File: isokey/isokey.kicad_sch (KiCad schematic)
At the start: 3 parts, among them J1 PadExp Left, J2 PadExp Right, U1 BlackPill_STLINK

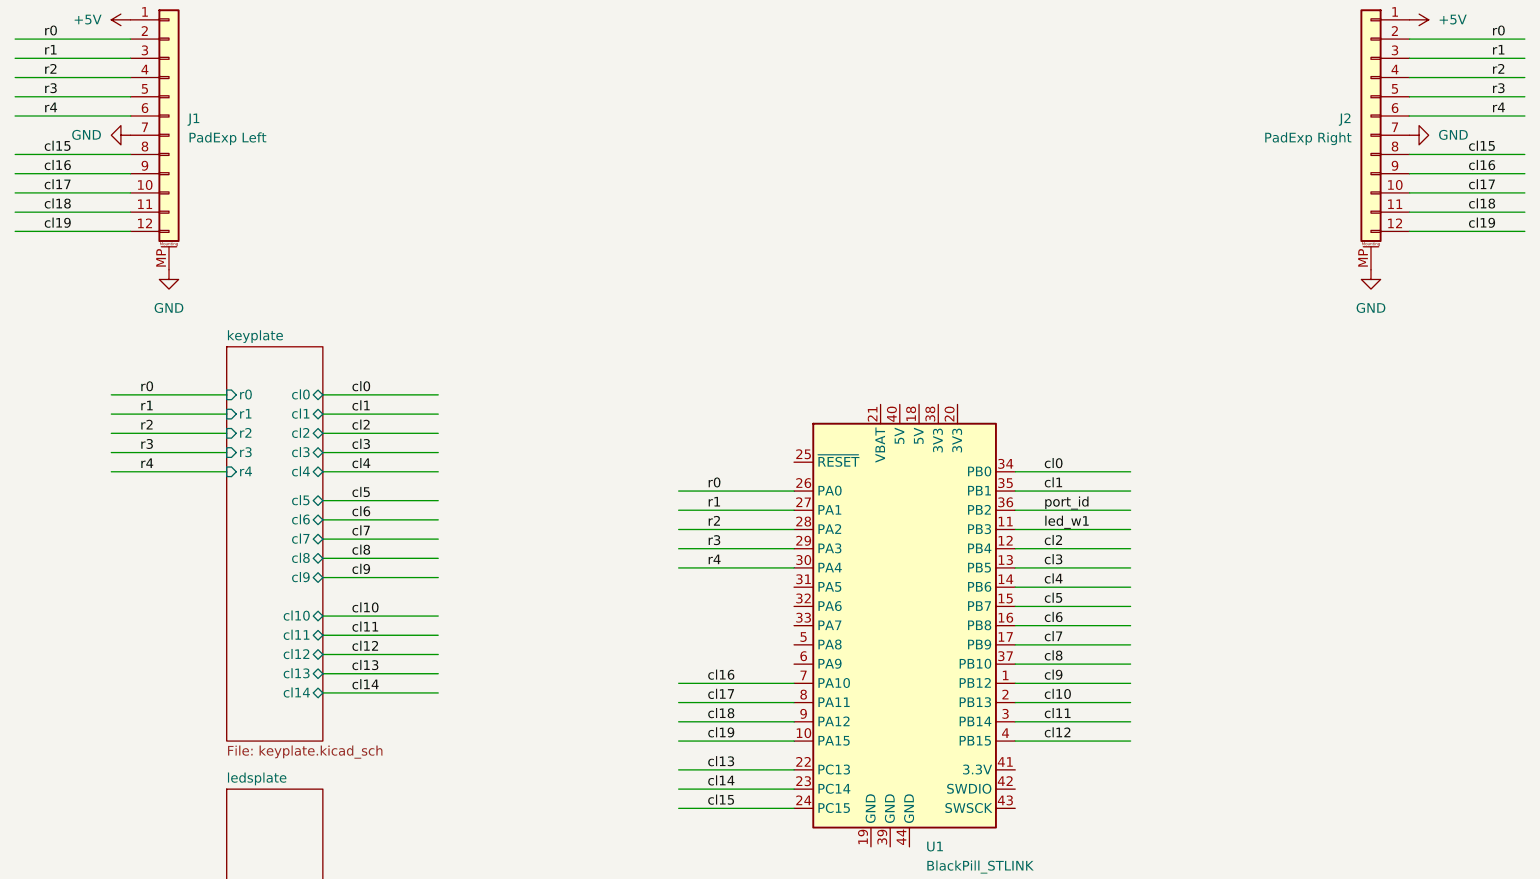
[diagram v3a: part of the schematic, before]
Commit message: Complete led wire
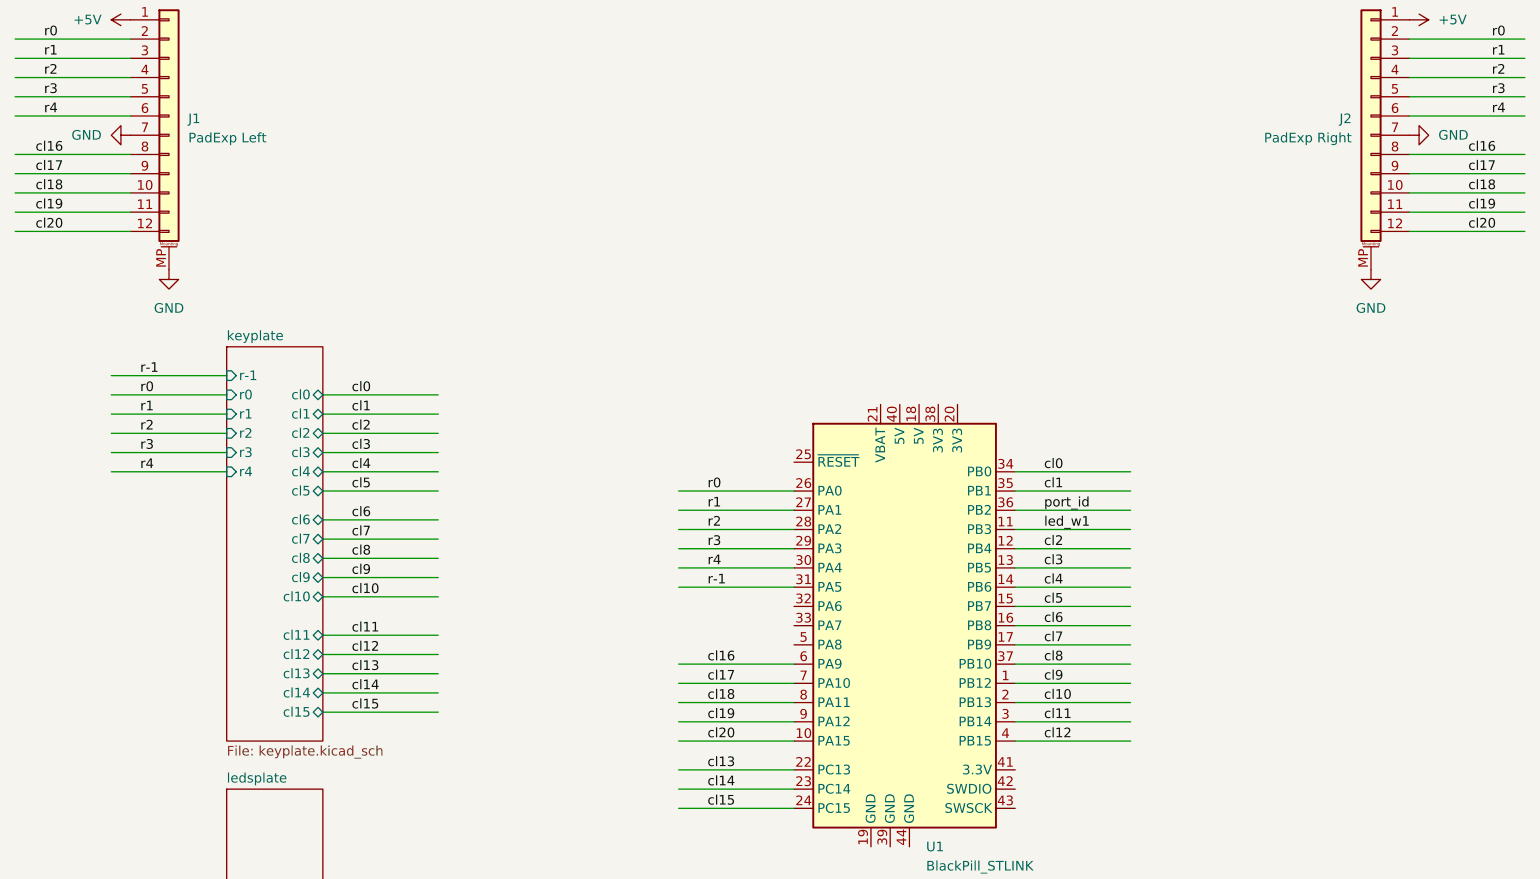
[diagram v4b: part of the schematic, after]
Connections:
- net cl15: no longer J1.8 (Pin_8), J2.8 (Pin_8)
- net cl16: now also J1.8 (Pin_8), J2.8 (Pin_8), U1.6 (PA9); no longer J1.9 (Pin_9), J2.9 (Pin_9), U1.7 (PA10)
- net cl17: now also J1.9 (Pin_9), J2.9 (Pin_9), U1.7 (PA10); no longer J1.10 (Pin_10), J2.10 (Pin_10), U1.8 (PA11)
- net cl18: now also J1.10 (Pin_10), J2.10 (Pin_10), U1.8 (PA11); no longer J1.11 (Pin_11), J2.11 (Pin_11), U1.9 (PA12)
- net cl19: now also J1.11 (Pin_11), J2.11 (Pin_11), U1.9 (PA12); no longer J1.12 (Pin_12), J2.12 (Pin_12), U1.10 (PA15)
- net r-1: now reaches U1.31 (PA5)
- new net cl20: J1.12 (Pin_12), J2.12 (Pin_12), U1.10 (PA15)
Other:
- sheet keyplate ports: added cl15, r-1; removed none

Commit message: Continue routing
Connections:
- net GND: now also U1.19 (GND), U1.39 (GND), U1.44 (GND)
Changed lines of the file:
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@@
     (company "IsoKey - asterix24@gmail.com")
   )
+  (junction (at 168.91 133.35) (diameter 0) (color 0 0 0 0)
+  )
+  (junction (at 171.45 133.35) (diameter 0) (color 0 0 0 0)
+  )
   (wire (pts (xy 187.96 93.98) (xy 203.2 93.98))
     (stroke (width 0) (type default))
@@
     (stroke (width 0) (type default))
   )
+  (wire (pts (xy 168.91 133.35) (xy 171.45 133.35))
+    (stroke (width 0) (type default))
+  )
   (wire (pts (xy 255.27 44.45) (xy 240.03 44.45))
     (stroke (width 0) (type default))
@@
   )
   (wire (pts (xy 96.52 105.41) (xy 111.76 105.41))
+    (stroke (width 0) (type default))
+  )
+  (wire (pts (xy 171.45 133.35) (xy 173.99 133.35))
     (stroke (width 0) (type default))
   )
@@
         )
       )
+    )
+  )
+  (symbol (lib_id "power:GND") (at 168.91 133.35 0) (unit 1)
+    (in_bom yes) (on_board yes) (dnp no) (fields_autoplaced)
+    (property "Reference" "#PWR0239" (at 168.91 139.7 0)
+      (effects (font (size 1.27 1.27)) hide)
+    )
+    (property "Value" "GND" (at 168.91 138.43 0)
+      (effects (font (size 1.27 1.27)))
+    )
+    (property "Footprint" "" (at 168.91 133.35 0)
+      (effects (font (size 1.27 1.27)) hide)
+    )
+    (property "Datasheet" "" (at 168.91 133.35 0)
+      (effects (font (size 1.27 1.27)) hide)
+    )
+    (pin "1")
+    (instances
+      (project "isokey"
+        (path "/b0c352a4-2db1-45ff-8668-f2efdeb7d408"
+          (reference "#PWR0239") (unit 1)
+        )
+      )

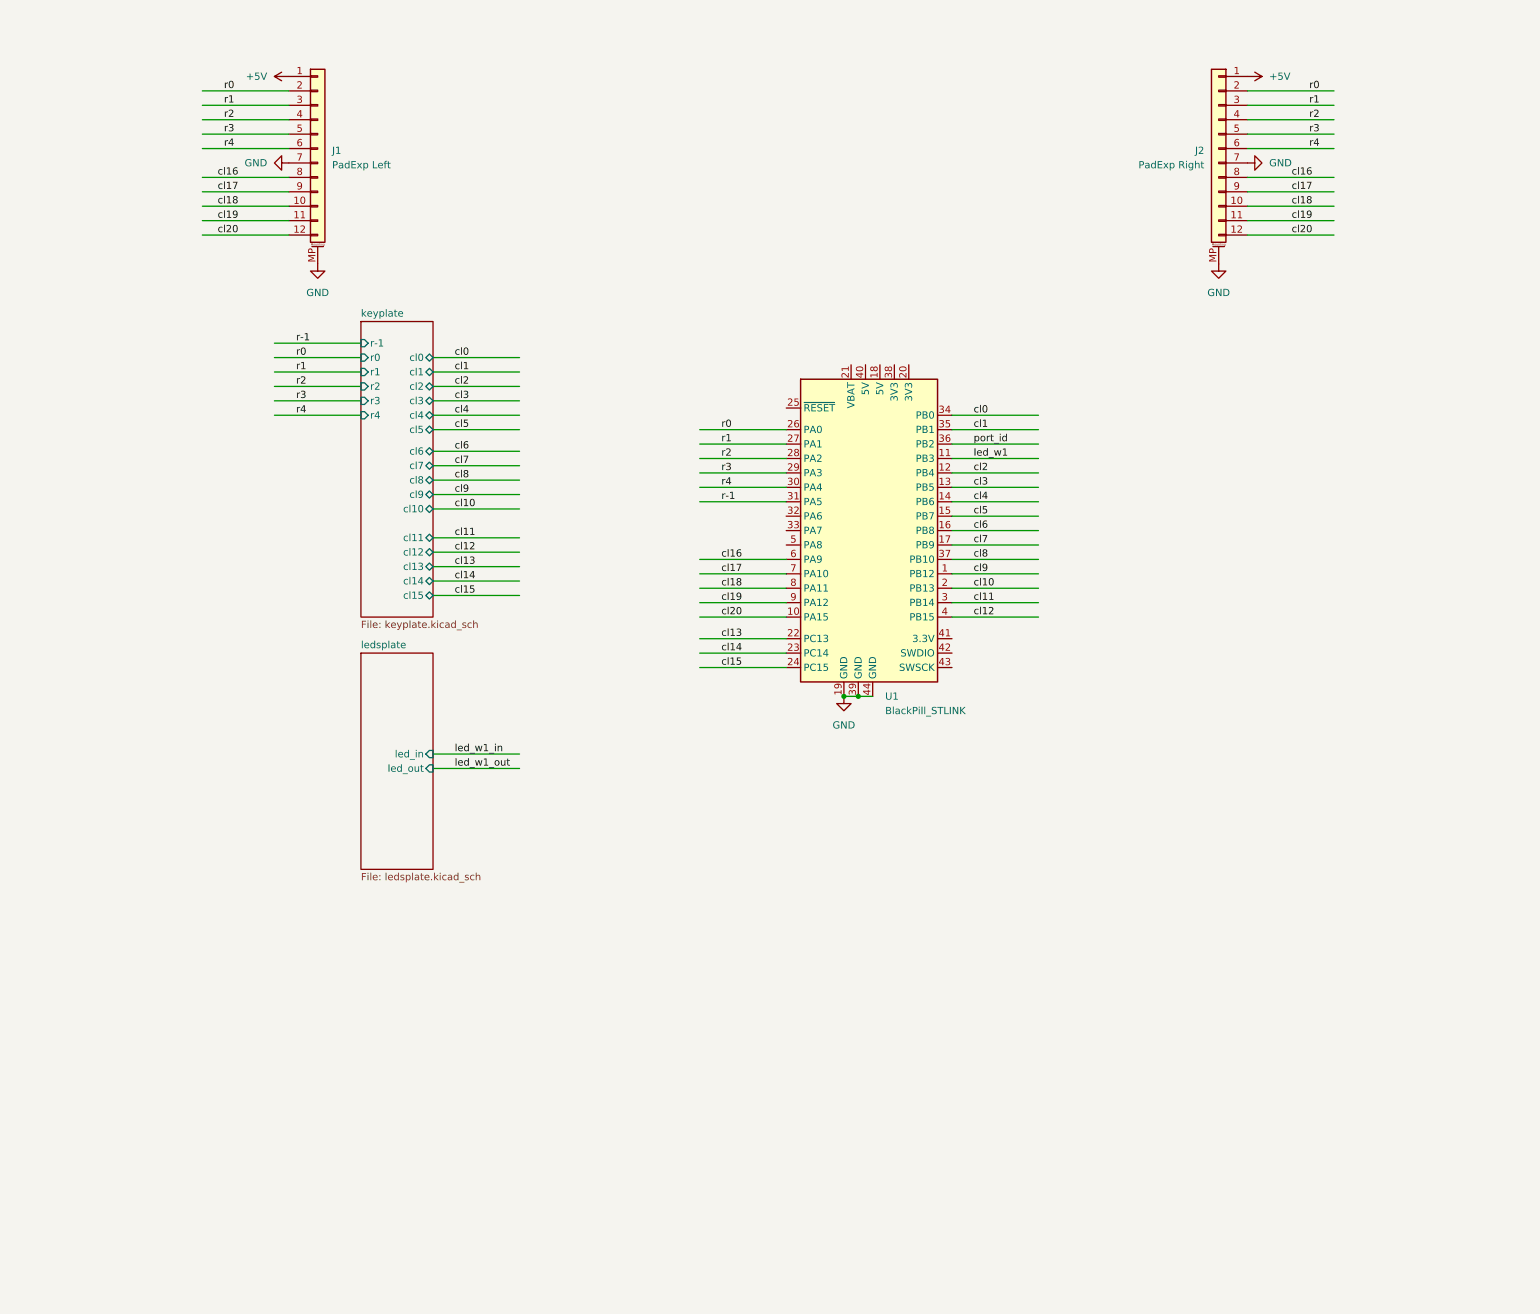
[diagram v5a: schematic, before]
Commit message: Add lp5569 chip and encoder.
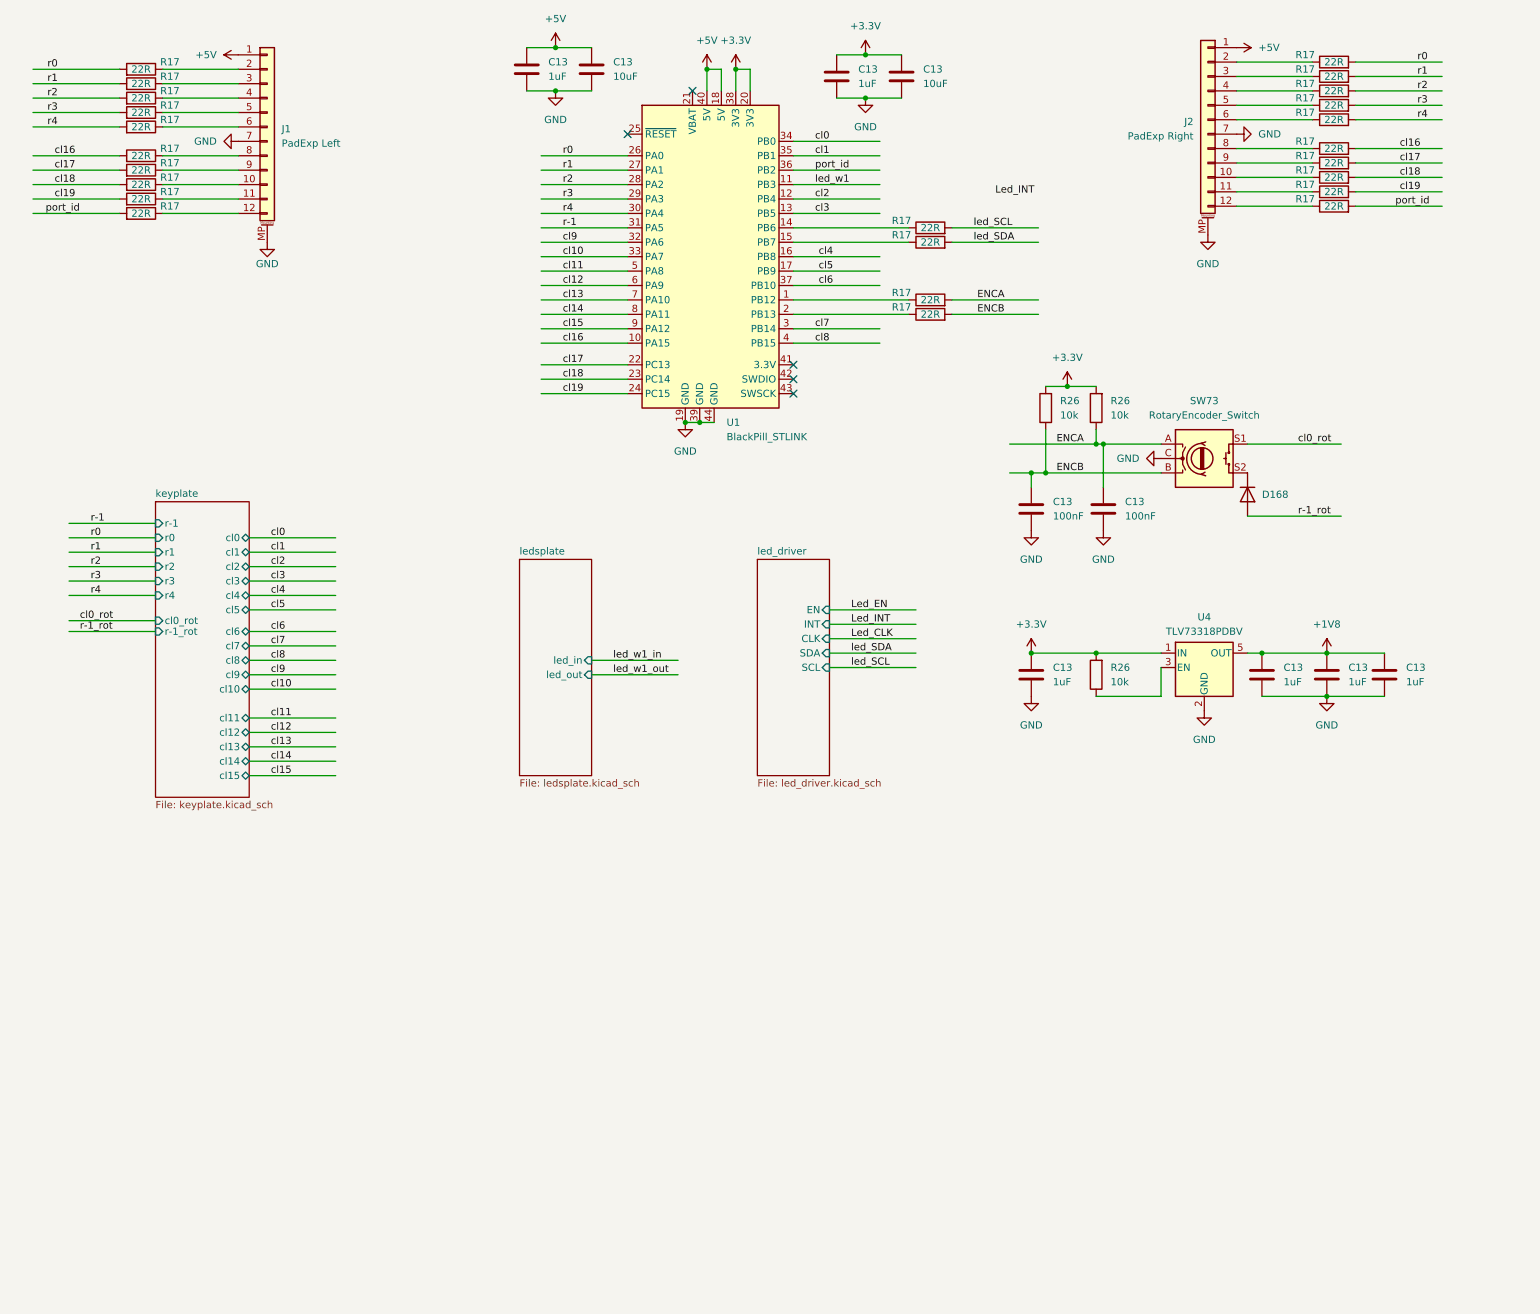
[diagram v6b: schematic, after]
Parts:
- added C13 (x6): 1uF, Capacitor_SMD:C_0805_2012Metric, symbol Device:C
- added C13 (x2): 10uF, Capacitor_SMD:C_1206_3216Metric, symbol Device:C
- added C13 (x2): 100nF, Capacitor_SMD:C_0603_1608Metric_Pad1.08x0.95mm_HandSolder, symbol Device:C
- added D168: 1N4448W, Diode_SMD:D_SOD-123, symbol Diode:1N4448W
- added R17 (x24): 22R, Resistor_SMD:R_0603_1608Metric_Pad0.98x0.95mm_HandSolder, symbol Device:R
- added R26 (x3): 10k, Resistor_SMD:R_0603_1608Metric_Pad0.98x0.95mm_HandSolder, symbol Device:R
- added SW73: RotaryEncoder_Switch, Rotary_Encoder:RotaryEncoder_Alps_EC12E-Switch_Vertical_H20mm_CircularMountingHoles, symbol Device:RotaryEncoder_Switch
- added U4: TLV73318PDBV, Package_TO_SOT_SMD:SOT-23-5, symbol Regulator_Linear:TLV73318PDBV
- U1: footprint Modules:BlackPill_STLINK -> Modules:BlackPill
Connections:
- net +5V: now also U1.18 (5V), U1.40 (5V), C13.1, C13.1
- net GND: now also C13.2, C13.2, C13.2, C13.2, C13.2, C13.2, C13.2, C13.2, C13.2, C13.2, SW73.C, U4.2 (GND)
- net cl10: now also U1.33 (PA7); no longer U1.2 (PB13)
- net cl11: now also U1.5 (PA8); no longer U1.3 (PB14)
- net cl12: now also U1.6 (PA9); no longer U1.4 (PB15)
- net cl13: now also U1.7 (PA10); no longer U1.22 (PC13)
- net cl14: now also U1.8 (PA11); no longer U1.23 (PC14)
- net cl15: now also U1.9 (PA12); no longer U1.24 (PC15)
- net cl16: now also U1.10 (PA15), R17.2, R17.2; no longer J1.8 (Pin_8), J2.8 (Pin_8), U1.6 (PA9)
- net cl17: now also U1.22 (PC13), R17.2, R17.2; no longer J1.9 (Pin_9), J2.9 (Pin_9), U1.7 (PA10)
- net cl18: now also U1.23 (PC14), R17.2, R17.2; no longer J1.10 (Pin_10), J2.10 (Pin_10), U1.8 (PA11)
- net cl19: now also U1.24 (PC15), R17.2, R17.2; no longer J1.11 (Pin_11), J2.11 (Pin_11), U1.9 (PA12)
- net cl4: now also U1.16 (PB8); no longer U1.14 (PB6)
- net cl5: now also U1.17 (PB9); no longer U1.15 (PB7)
- net cl6: now also U1.37 (PB10); no longer U1.16 (PB8)
- net cl7: now also U1.3 (PB14); no longer U1.17 (PB9)
- net cl8: now also U1.4 (PB15); no longer U1.37 (PB10)
- net cl9: now also U1.32 (PA6); no longer U1.1 (PB12)
- net port_id: now also R17.2, R17.2
- net r0: now also R17.2, R17.2; no longer J1.2 (Pin_2), J2.2 (Pin_2)
- net r1: now also R17.2, R17.2; no longer J1.3 (Pin_3), J2.3 (Pin_3)
- net r2: now also R17.2, R17.2; no longer J1.4 (Pin_4), J2.4 (Pin_4)
- net r3: now also R17.2, R17.2; no longer J1.5 (Pin_5), J2.5 (Pin_5)
- net r4: now also R17.2, R17.2; no longer J1.6 (Pin_6), J2.6 (Pin_6)
- net +3.3V: now reaches U1.20 (3V3)
- net +3.3V: now also U1.38 (3V3), C13.1, C13.1, C13.1, R26.2, R26.2, R26.2, U4.1 (IN)
- removed net cl20: J1.12 (Pin_12), J2.12 (Pin_12), U1.10 (PA15)
- new net: J2.12 (Pin_12), R17.1
- new net: R17.1, U1.2 (PB13)
- new net: J2.8 (Pin_8), R17.1
- new net: D168.1 (K), SW73.S2
- new net: J1.8 (Pin_8), R17.1
- new net: J1.10 (Pin_10), R17.1
- new net: J2.3 (Pin_3), R17.1
- new net: R26.1, U4.3 (EN)
- new net: J2.9 (Pin_9), R17.1
- new net: J1.5 (Pin_5), R17.1
- new net: J2.11 (Pin_11), R17.1
- new net: J1.9 (Pin_9), R17.1
- new net: R17.1, U1.14 (PB6)
- new net: R17.1, U1.15 (PB7)
- new net: J1.11 (Pin_11), R17.1
- new net: J2.4 (Pin_4), R17.1
- new net: J2.5 (Pin_5), R17.1
- new net: J2.10 (Pin_10), R17.1
- new net: J1.12 (Pin_12), R17.1
- new net: J1.2 (Pin_2), R17.1
- new net: J1.3 (Pin_3), R17.1
- new net: J1.4 (Pin_4), R17.1
- new net: J1.6 (Pin_6), R17.1
- new net: J2.2 (Pin_2), R17.1
- new net: J2.6 (Pin_6), R17.1
- new net: R17.1, U1.1 (PB12)
- new net +1V8: C13.1, C13.1, C13.1, U4.5 (OUT)
- new net ENCA: C13.1, R17.2, R26.1, SW73.A
- new net ENCB: C13.1, R17.2, R26.1, SW73.B
- new net cl0_rot: SW73.S1
- new net led_SCL: R17.2
- new net led_SDA: R17.2
- new net r-1_rot: D168.2 (A)
- no-connect marks 0 -> 5
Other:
- added sheet led_driver (led_driver.kicad_sch)
- sheet keyplate ports: added cl0_rot, r-1_rot; removed none
- moved on the sheet: J1, J2, U1
